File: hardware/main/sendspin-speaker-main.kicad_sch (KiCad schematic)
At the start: 0 parts

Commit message: hardware: main board block diagram (five hierarchical sheets)
Co-Authored-By: Claude Opus 5.5 <noreply@anthropic.com>
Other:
- added sheet Audio (audio.kicad_sch)
- added sheet Connectors (connectors.kicad_sch)
- added sheet MCU (mcu.kicad_sch)
- added sheet Power (power.kicad_sch)
- added sheet USB (usb.kicad_sch)
- note added: "Block diagram. Rails are global power symbols inside the sheets: VBUS (USB 5 V), VBAT (protected cell), VBAT_SW (after the on/off switch), +3V3 (ESP32-A1S), +3V3_USB (CH340C only), GND. SMD passives and LEDs 0805 wherever possible."

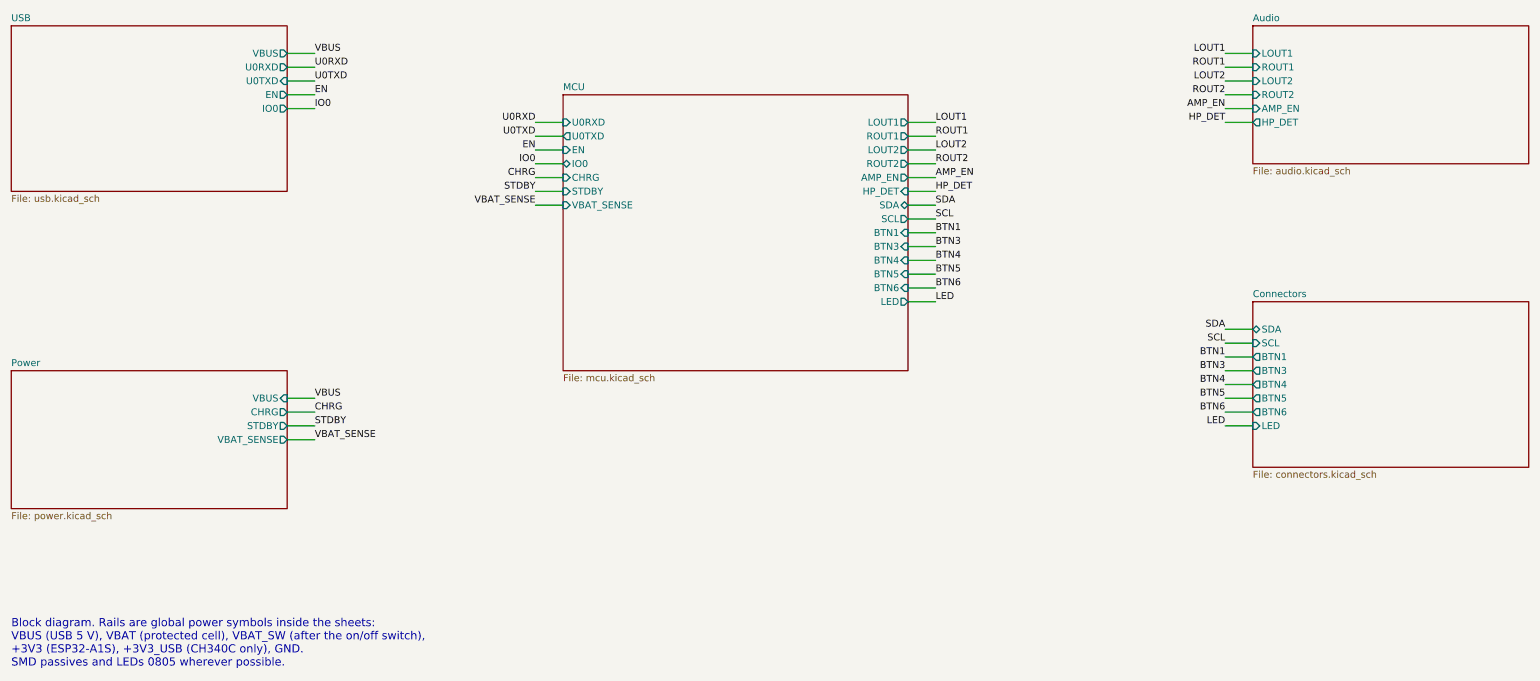
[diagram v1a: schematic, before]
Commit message: hardware: footprints for every part, LCSC library, real A1S pin plan
- lib/lcsc: ESP32-A1S, NS4150B, FS8205A, MSK12C02, PJ-320D imported
  from LCSC with easyeda2kicad (3D paths fixed, NPTH pegs, A1S antenna
  keepout and courtyard), registered in all three projects.
- Parts table with footprint and LCSC number in hardware/README.md.
- The A1S keeps the codec's I2C/I2S inside: display moves to the
  ST7789's pins 14/13/15/22 (SPI or I2C), LED to 12, CHRG/STDBY to 4/2
  through BAT54W. J_SW and J_CHG for an off-board switch and charge LEDs.
- Block sheets use the module's real outputs (HPOUTL/R, SPOLP/N, SPORP/N).

Co-Authored-By: Claude Opus 5.5 <noreply@anthropic.com>
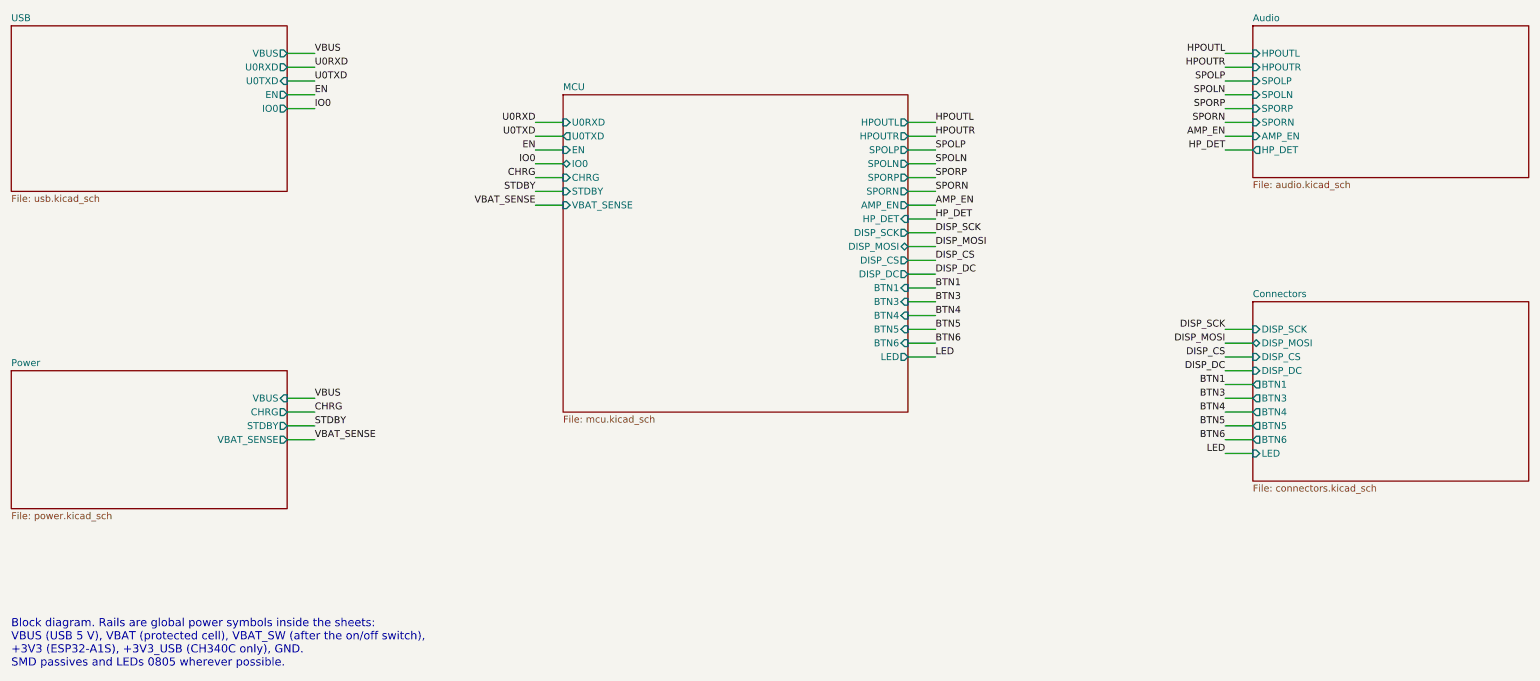
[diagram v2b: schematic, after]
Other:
- sheet Audio ports: added HPOUTL, HPOUTR, SPOLN, SPOLP, SPORN, SPORP; removed LOUT1, LOUT2, ROUT1, ROUT2
- sheet Connectors ports: added DISP_CS, DISP_DC, DISP_MOSI, DISP_SCK; removed SCL, SDA
- sheet MCU ports: added DISP_CS, DISP_DC, DISP_MOSI, DISP_SCK, HPOUTL, HPOUTR, SPOLN, SPOLP, SPORN, SPORP; removed LOUT1, LOUT2, ROUT1, ROUT2, SCL, SDA

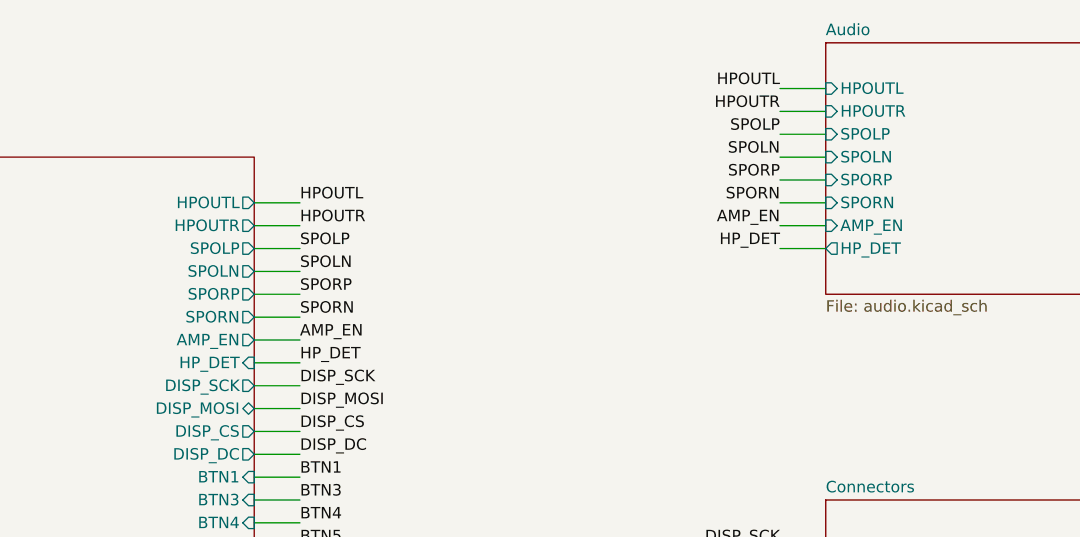
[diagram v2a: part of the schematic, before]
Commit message: hardware: headphone jack removed, main board 70 x 60 mm
- J403, C422, C423 out; HPOUTL/R open, GPIO39 spare with its pull-up.
- Main board re-placed on 70 x 60 mm (decoupling placed first), routed,
  labelled; route.py cleans dangling vias and sub-minimum tracks.
- LCSC fields rewritten after regenerating MCU and Audio sheets.

Co-Authored-By: Claude Opus 5.5 <noreply@anthropic.com>
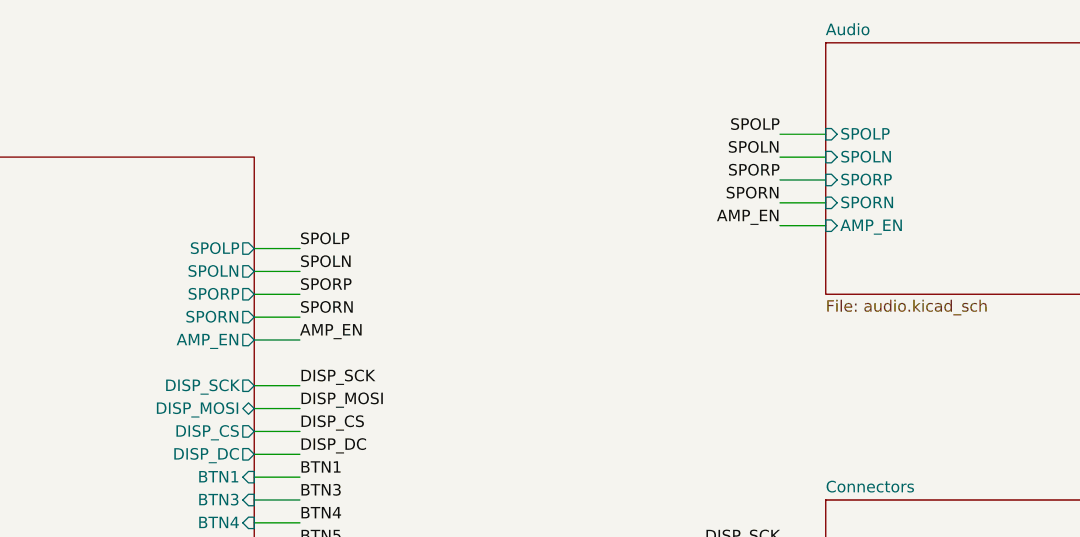
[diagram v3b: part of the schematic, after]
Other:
- sheet Audio ports: added none; removed HPOUTL, HPOUTR, HP_DET
- sheet MCU ports: added none; removed HPOUTL, HPOUTR, HP_DET
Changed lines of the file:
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@@
-	(wire
-		(pts
-			(xy 274.32 55.88) (xy 279.4 55.88)
-		)
-		(stroke
-			(width 0)
-			(type default)
-		)
-	)
 	(wire
 		(pts
@@
 	(wire
 		(pts
-			(xy 274.32 73.66) (xy 279.4 73.66)
-		)
-		(stroke
-			(width 0)
-			(type default)
-		)
-	)
-	(wire
-		(pts
 			(xy 215.9 76.2) (xy 220.98 76.2)
 		)
@@
 	(wire
 		(pts
-			(xy 215.9 71.12) (xy 220.98 71.12)
-		)
-		(stroke
-			(width 0)
-			(type default)
-		)
-	)
-	(wire
-		(pts
-			(xy 215.9 86.36) (xy 220.98 86.36)
-		)
-		(stroke
-			(width 0)
-			(type default)
-		)
-	)
-	(wire
-		(pts
 			(xy 215.9 81.28) (xy 220.98 81.28)
 		)
@@
 	(wire
 		(pts
-			(xy 215.9 68.58) (xy 220.98 68.58)
-		)
-		(stroke
-			(width 0)
-			(type default)
-		)
-	)
-	(wire
-		(pts
 			(xy 101.6 58.42) (xy 106.68 58.42)
 		)
@@
 		(pts
 			(xy 215.9 78.74) (xy 220.98 78.74)
-		)
-		(stroke
-			(width 0)
-			(type default)
-		)
-	)
-	(wire
-		(pts
-			(xy 274.32 58.42) (xy 279.4 58.42)
 		)
 		(stroke
@@
 		)
 	)
-	(label "HP_DET"
-		(at 220.98 86.36 0)
-		(effects
-			(font
-				(size 1.27 1.27)
-			)
-			(justify left bottom)
-		)
-	)
 	(label "SPORP"
 		(at 220.98 78.74 0)
@@
 		)
 	)
-	(label "HP_DET"
-		(at 274.32 73.66 180)
-		(effects
-			(font
-				(size 1.27 1.27)
-			)
-			(justify right bottom)
-		)
-	)
 	(label "DISP_MOSI"
 		(at 220.98 91.44 0)
@@
 		)
 	)
-	(label "HPOUTL"
-		(at 274.32 55.88 180)
-		(effects
-			(font
-				(size 1.27 1.27)
-			)
-			(justify right bottom)
-		)
-	)
-	(label "HPOUTR"
-		(at 274.32 58.42 180)
-		(effects
-			(font
-				(size 1.27 1.27)
-			)
-			(justify right bottom)
-		)
-	)
 	(label "DISP_MOSI"
 		(at 274.32 109.22 180)
@@
 		)
 	)
-	(label "HPOUTL"
-		(at 220.98 68.58 0)
-		(effects
-			(font
-				(size 1.27 1.27)
-			)
-			(justify left bottom)
-		)
-	)
 	(label "DISP_CS"
 		(at 274.32 111.76 180)
@@
 	(label "U0RXD"
 		(at 106.68 58.42 0)
-		(effects
-			(font
-				(size 1.27 1.27)
-			)
-			(justify left bottom)
-		)
-	)
-	(label "HPOUTR"
-		(at 220.98 71.12 0)
 		(effects
 			(font
@@
 			)
 		)
-		(pin "HPOUTL" input
-			(at 279.4 55.88 180)
-			(effects
-				(font
-					(size 1.27 1.27)
-				)
-				(justify left)
-			)
-		)
-		(pin "HPOUTR" input
-			(at 279.4 58.42 180)
-			(effects
-				(font
-					(size 1.27 1.27)
-				)
-				(justify left)
-			)
-		)
 		(pin "SPOLP" input
 			(at 279.4 60.96 180)
@@
 		(pin "AMP_EN" input
 			(at 279.4 71.12 180)
-			(effects
-				(font
-					(size 1.27 1.27)
-				)
-				(justify left)
-			)
-		)
-		(pin "HP_DET" output
-			(at 279.4 73.66 180)
 			(effects
 				(font
@@
 			)
 		)
-		(pin "HPOUTL" output
-			(at 215.9 68.58 0)
-			(effects
-				(font
-					(size 1.27 1.27)
-				)
-				(justify right)
-			)
-		)
-		(pin "HPOUTR" output
-			(at 215.9 71.12 0)
-			(effects
-				(font
-					(size 1.27 1.27)
-				)
-				(justify right)
-			)
-		)
 		(pin "SPOLP" output
 			(at 215.9 73.66 0)
@@
 			(effects
 				(font
-					(size 1.27 1.27)
-				)
-				(justify right)
-			)
-		)
-		(pin "HP_DET" input
-			(at 215.9 86.36 0)
-			(effects
-				(font
